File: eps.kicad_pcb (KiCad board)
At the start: 4 copper layers, 95.9 x 90.2 mm, 141 parts, among them J1 CONN_01X05, J2 CONN_01X05, J3 CONN_01X05, J4 CONN_01X05, J5 +BATT, J6 -BATT, J7 PROGRAMMING PORT, J8 H_EPS, J9 DEBUG, Q1 BSC026NE2LS5, Q2 BSC026NE2LS5, Q3 BSC026NE2LS5, Q4 BSC026NE2LS5, Q5 BSC026NE2LS5, Q6 BSC026NE2LS5, SW1 SW_RST, U1 ATMEGA32M1-MU, U10 ADS7952, U11 TPS630250, U12 bq297xx, U13 INA214, U14 INA214, U15 TPS630250, U16 TPS61088, U17 TPS61088, U18 ADS7952, U19 INA214, U2 INA214, U20 INA214, U21 INA214, U22 REF5025, U23 REF5025, U3 INA214, U4 INA214, U5 INA214, U6 ADA4891-4, U7 ADA4891-4, U8 SN65HVD230, U9 SST25VF016B, Y1 8MHz

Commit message: Merge remote-tracking branch 'origin/master'
# Conflicts:
#	Board.zip
#	Board/eps-B.Cu.gbr
#	Board/eps-B.Mask.gbr
#	Board/eps-B.SilkS.gbr
#	Board/eps-Edge.Cuts.gbr
#	Board/eps-F.Cu.gbr
#	Board/eps-F.Mask.gbr
#	Board/eps-F.SilkS.gbr
#	Board/eps-GND.gbr
#	Board/eps-VCC.gbr
#	Board/eps.drl
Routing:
- net GND: track 327.1 -> 335.0 mm, vias 56 -> 63
- net (no net): vias 4 -> 0
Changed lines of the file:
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@@
     (links 467)
     (no_connects 44)
-    (area 100.034999 49.754999 196.075001 140.075001)
+    (area 98.589999 47.237143 197.520002 141.520002)
     (thickness 1.6)
     (drawings 5)
-    (tracks 1822)
+    (tracks 1832)
     (zones 0)
     (modules 141)
@@
       (padsonsilk false)
       (subtractmaskfromsilk false)
-      (outputformat 2)
+      (outputformat 1)
       (mirror false)
       (drillshape 0)
@@
   (gr_line (start 196 49.83) (end 100.11 49.83) (angle 90) (layer Edge.Cuts) (width 0.15))
   (gr_line (start 196 49.83) (end 196 140) (angle 90) (layer Edge.Cuts) (width 0.15))
-  (via (at 105.19 131.11) (size 6.4) (drill 3.2) (layers F.Cu B.Cu) (net 0))
-  (via (at 105.19 57.45) (size 6.4) (drill 3.2) (layers F.Cu B.Cu) (net 0))
-  (via (at 190.92 134.92) (size 6.4) (drill 3.2) (layers F.Cu B.Cu) (net 0))
-  (via (at 190.92 54.91) (size 6.4) (drill 3.2) (layers F.Cu B.Cu) (net 0))
+  (via (at 105.19 131.11) (size 6.4) (drill 3.2) (layers F.Cu B.Cu) (net 1))
+  (via (at 190.92 54.91) (size 6.4) (drill 3.2) (layers F.Cu B.Cu) (net 1))
+  (segment (start 188.9 74.13) (end 188.9 73.405) (width 0.25) (layer F.Cu) (net 1))
+  (via (at 190.92 134.92) (size 6.4) (drill 3.2) (layers F.Cu B.Cu) (net 1))
+  (via (at 105.19 57.45) (size 6.4) (drill 3.2) (layers F.Cu B.Cu) (net 1))
+  (segment (start 106.35 112.31) (end 106.35 108.59) (width 0.25) (layer F.Cu) (net 1))
+  (segment (start 106.35 108.59) (end 106.67 108.27) (width 0.25) (layer F.Cu) (net 1))
+  (via (at 106.67 108.27) (size 0.6) (drill 0.3) (layers F.Cu B.Cu) (net 1))
+  (segment (start 106.35 117.31) (end 106.35 118.11) (width 0.25) (layer F.Cu) (net 1))
+  (segment (start 106.35 118.11) (end 106.67 118.43) (width 0.25) (layer F.Cu) (net 1))
+  (via (at 106.67 118.43) (size 0.6) (drill 0.3) (layers F.Cu B.Cu) (net 1))
+  (segment (start 106.35 74.13) (end 106.35 73.03) (width 0.25) (layer F.Cu) (net 1))
+  (segment (start 106.35 73.03) (end 106.67 72.71) (width 0.25) (layer F.Cu) (net 1))
+  (via (at 106.67 72.71) (size 0.6) (drill 0.3) (layers F.Cu B.Cu) (net 1))
+  (segment (start 188.9 117.23) (end 188.9 120.02) (width 0.25) (layer F.Cu) (net 1))
+  (segment (start 188.9 120.02) (end 187.95 120.97) (width 0.25) (layer F.Cu) (net 1))
+  (via (at 187.95 120.97) (size 0.6) (drill 0.3) (layers F.Cu B.Cu) (net 1))
+  (segment (start 188.9 112.23) (end 191.61 112.23) (width 0.25) (layer F.Cu) (net 1))
+  (segment (start 191.61 112.23) (end 193.03 110.81) (width 0.25) (layer F.Cu) (net 1))
+  (via (at 193.03 110.81) (size 0.6) (drill 0.3) (layers F.Cu B.Cu) (net 1))
+  (segment (start 188.9 79.13) (end 188.9 81.92) (width 0.25) (layer F.Cu) (net 1))
+  (segment (start 188.9 81.92) (end 187.95 82.87) (width 0.25) (layer F.Cu) (net 1))
+  (via (at 187.95 82.87) (size 0.6) (drill 0.3) (layers F.Cu B.Cu) (net 1))
   (segment (start 138.73754 84.60496) (end 138.73754 84.12998) (width 0.25) (layer F.Cu) (net 1))
   (segment (start 136.35756 81.75) (end 136.26 81.75) (width 0.25) (layer F.Cu) (net 1))
@@
   (segment (start 153.08 56.09) (end 152.07 55.08) (width 0.25) (layer F.Cu) (net 1))
   (via (at 152.07 55.08) (size 0.6) (drill 0.3) (layers F.Cu B.Cu) (net 1))
-  (segment (start 106.35 74.13) (end 106.35 71.59) (width 0.25) (layer GND) (net 1))
-  (via (at 106.35 71.59) (size 0.6) (drill 0.3) (layers F.Cu B.Cu) (net 1))
   (segment (start 106.35 79.13) (end 106.35 81.75) (width 0.25) (layer F.Cu) (net 1))
   (via (at 106.35 81.75) (size 0.6) (drill 0.3) (layers F.Cu B.Cu) (net 1))
@@
   (segment (start 135.56 81.75) (end 133.65 81.75) (width 0.25) (layer F.Cu) (net 1))
   (segment (start 133.65 81.75) (end 133.02 81.12) (width 0.25) (layer F.Cu) (net 1))
-  (segment (start 188.9 79.13) (end 188.9 80.48) (width 0.25) (layer GND) (net 1))
   (segment (start 188.9 74.13) (end 188.9 73.113874) (width 0.25) (layer F.Cu) (net 1))
   (segment (start 188.9 73.113874) (end 188.773063 72.986937) (width 0.25) (layer F.Cu) (net 1))
   (via (at 188.773063 72.986937) (size 0.6) (drill 0.3) (layers F.Cu B.Cu) (net 1))
   (via (at 188.9 74.13) (size 0.6) (drill 0.3) (layers F.Cu B.Cu) (net 1))
-  (segment (start 190.17 112.23) (end 188.9 112.23) (width 0.25) (layer F.Cu) (net 1))
-  (segment (start 190.17 118.58) (end 190.17 116.88) (width 0.25) (layer B.Cu) (net 1))
-  (segment (start 190.17 116.88) (end 190.17 112.23) (width 0.25) (layer B.Cu) (net 1))
-  (via (at 190.17 112.23) (size 0.6) (drill 0.3) (layers F.Cu B.Cu) (net 1))
-  (segment (start 188.9 118.58) (end 190.17 118.58) (width 0.25) (layer B.Cu) (net 1))
   (segment (start 188.9 117.23) (end 188.9 118.58) (width 0.25) (layer F.Cu) (net 1))
-  (via (at 188.9 118.58) (size 0.6) (drill 0.3) (layers F.Cu B.Cu) (net 1))
   (via (at 188.9 117.23) (size 0.6) (drill 0.3) (layers F.Cu B.Cu) (net 1))
   (via (at 188.9 117.23) (size 0.6) (drill 0.3) (layers F.Cu B.Cu) (net 1))
@@
   (segment (start 105.08 120.29) (end 105.08 108.4) (width 0.25) (layer F.Cu) (net 137))
   (segment (start 105.08 108.4) (end 106.35 107.13) (width 0.25) (layer F.Cu) (net 137))
-  (segment (start 109.009968 59.71) (end 109.009968 58.770032) (width 0.25) (layer F.Cu) (net 138))
-  (segment (start 109.009968 58.770032) (end 110.16 57.62) (width 0.25) (layer F.Cu) (net 138))
-  (segment (start 108.119869 71.520131) (end 108.119869 60.600099) (width 0.25) (layer F.Cu) (net 138))
-  (segment (start 108.119869 60.600099) (end 109.009968 59.71) (width 0.25) (layer F.Cu) (net 138))
-  (segment (start 107.62 71.578616) (end 108.061384 71.578616) (width 0.25) (layer F.Cu) (net 138))
-  (segment (start 108.061384 71.578616) (end 108.119869 71.520131) (width 0.25) (layer F.Cu) (net 138))
+  (segment (start 110.16 57.62) (end 109.009968 58.770032) (width 0.25) (layer F.Cu) (net 138))
+  (segment (start 109.009968 58.770032) (end 109.009968 59.71) (width 0.25) (layer F.Cu) (net 138))
+  (segment (start 106.369999 72.084999) (end 105.39999 73.055008) (width 0.25) (layer F.Cu) (net 138))
+  (segment (start 109.009968 59.71) (end 108.119869 60.600099) (width 0.25) (layer F.Cu) (net 138))
+  (segment (start 105.39999 73.055008) (end 105.39999 83.88499) (width 0.25) (layer F.Cu) (net 138))
+  (segment (start 108.119869 60.600099) (end 108.119869 71.520131) (width 0.25) (layer F.Cu) (net 138))
+  (segment (start 107.555001 72.084999) (end 106.369999 72.084999) (width 0.25) (layer F.Cu) (net 138))
+  (segment (start 108.119869 71.520131) (end 107.555001 72.084999) (width 0.25) (layer F.Cu) (net 138))
+  (segment (start 105.39999 83.88499) (end 106.35 84.835) (width 0.25) (layer F.Cu) (net 138))
+  (segment (start 106.35 84.835) (end 106.35 85.56) (width 0.25) (layer F.Cu) (net 138))
   (segment (start 107.62 83.02) (end 107.62 84.44) (width 0.25) (layer F.Cu) (net 138))
   (segment (start 107.62 84.44) (end 106.5 85.56) (width 0.25) (layer F.Cu) (net 138))
@@
   (segment (start 114.19 62.68) (end 111.37 62.68) (width 0.25) (layer B.Cu) (net 138))
   (segment (start 111.37 62.68) (end 111.34 62.71) (width 0.25) (layer B.Cu) (net 138))
-  (segment (start 106.35 85.56) (end 106.35 84.835) (width 0.25) (layer F.Cu) (net 138))
-  (segment (start 106.35 84.835) (end 105.39999 83.88499) (width 0.25) (layer F.Cu) (net 138))
-  (segment (start 105.39999 83.88499) (end 105.39999 73.798626) (width 0.25) (layer F.Cu) (net 138))
-  (segment (start 105.39999 73.798626) (end 107.62 71.578616) (width 0.25) (layer F.Cu) (net 138))
   (segment (start 110.16 57.62) (end 111.15 58.61) (width 0.25) (layer B.Cu) (net 138))
   (segment (start 111.15 58.61) (end 114.19 58.61) (width 0.25) (layer B.Cu) (net 138))

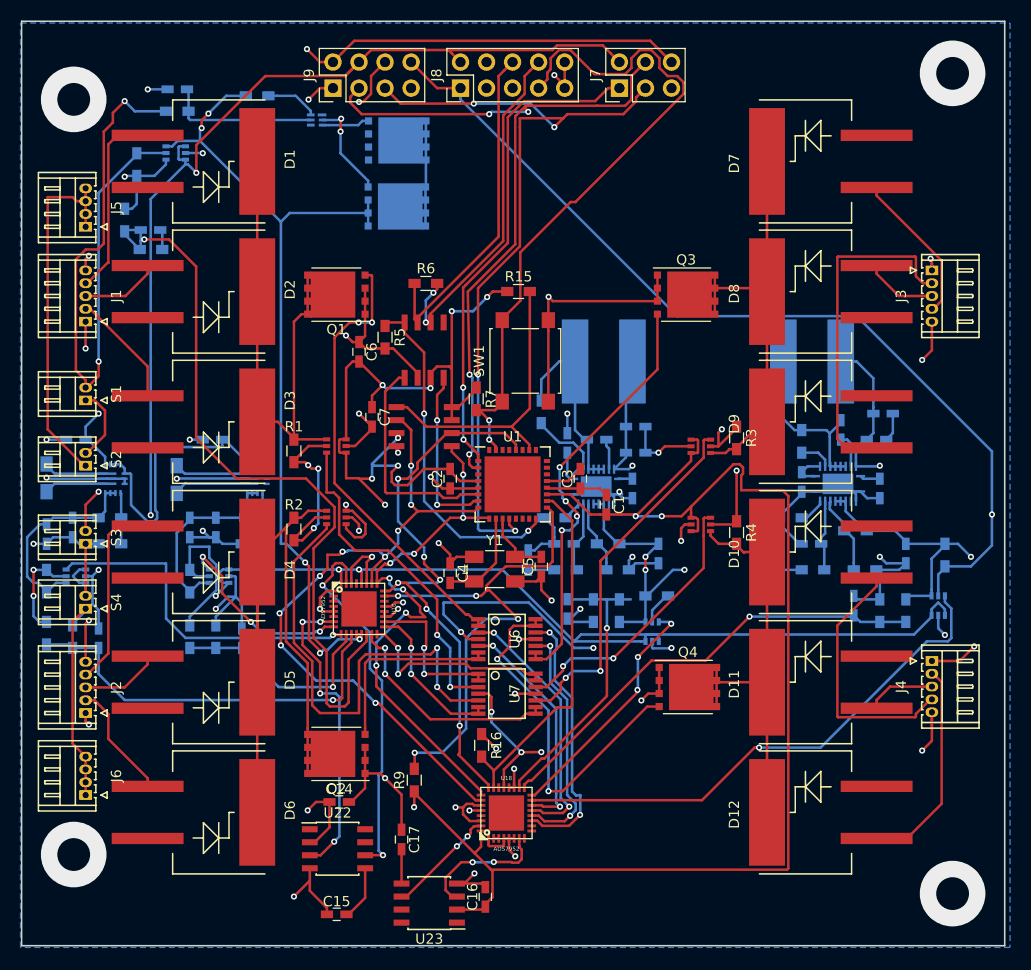
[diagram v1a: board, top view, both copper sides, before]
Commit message: Ground Pour, Pad Clearance
Fixed the ground pour, fixed pad clearances on connectors because DFMcheck was mad about it
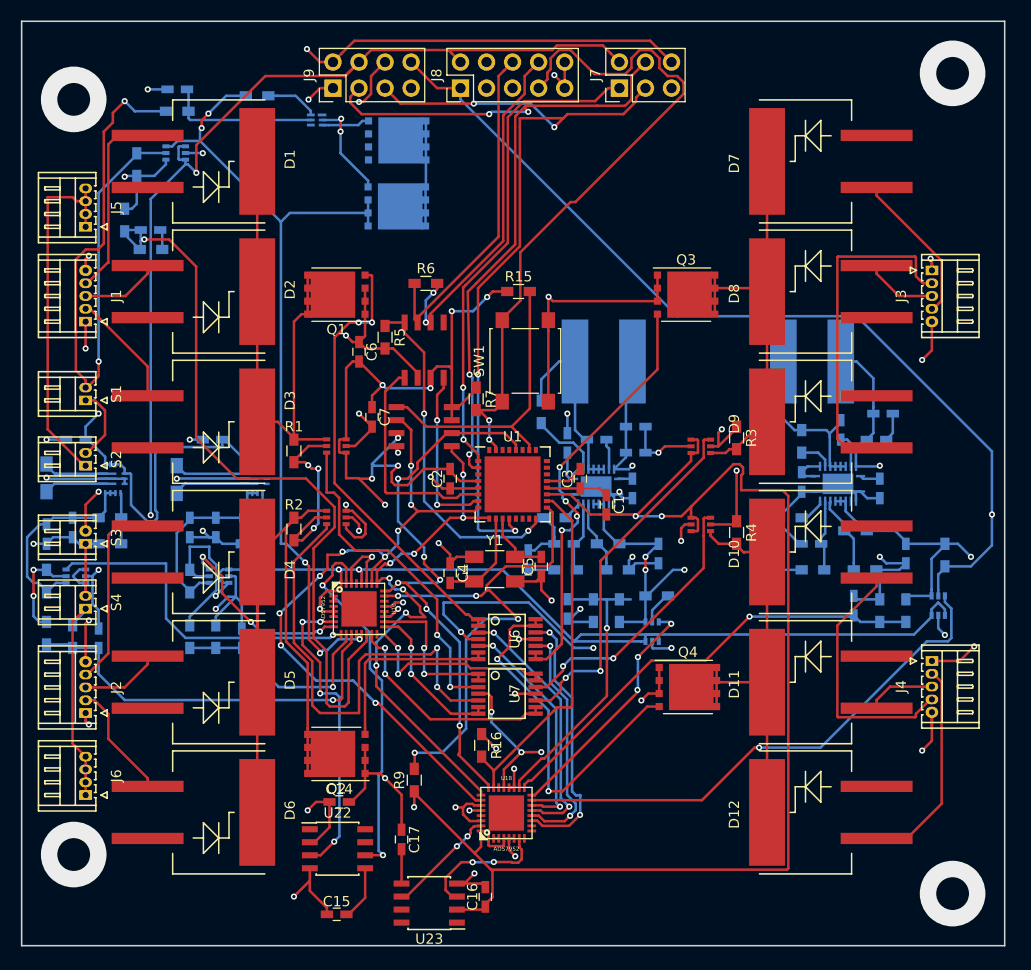
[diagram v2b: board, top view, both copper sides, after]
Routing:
- net GND: vias 63 -> 59
- net (no net): vias 0 -> 4
- added copper zone on GND, net GND
- removed copper zone on B.Cu, net GND
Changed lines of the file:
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@@
-(kicad_pcb (version 4) (host pcbnew 4.0.7)
+(kicad_pcb (version 4) (host pcbnew 4.0.6)
   (general
     (links 467)
-    (no_connects 44)
+    (no_connects 33)
     (area 98.589999 47.237143 197.520002 141.520002)
     (thickness 1.6)
@@
     (2 GND power)
     (31 B.Cu signal)
-    (32 B.Adhes user)
-    (33 F.Adhes user)
-    (34 B.Paste user)
-    (35 F.Paste user)
-    (36 B.SilkS user)
-    (37 F.SilkS user)
-    (38 B.Mask user)
-    (39 F.Mask user)
-    (40 Dwgs.User user)
-    (41 Cmts.User user)
-    (42 Eco1.User user)
-    (43 Eco2.User user)
+    (32 B.Adhes user hide)
+    (33 F.Adhes user hide)
+    (34 B.Paste user hide)
+    (35 F.Paste user hide)
+    (36 B.SilkS user hide)
+    (37 F.SilkS user hide)
+    (38 B.Mask user hide)
+    (39 F.Mask user hide)
+    (40 Dwgs.User user hide)
+    (41 Cmts.User user hide)
+    (42 Eco1.User user hide)
+    (43 Eco2.User user hide)
     (44 Edge.Cuts user)
-    (45 Margin user)
-    (46 B.CrtYd user)
-    (47 F.CrtYd user)
-    (48 B.Fab user)
-    (49 F.Fab user)
+    (45 Margin user hide)
+    (46 B.CrtYd user hide)
+    (47 F.CrtYd user hide)
+    (48 B.Fab user hide)
+    (49 F.Fab user hide)
   )
   (setup
@@
     (mod_text_size 1 1)
     (mod_text_width 0.15)
-    (pad_size 11 11)
-    (pad_drill 6.4)
+    (pad_size 1.1 1.25)
+    (pad_drill 0.6)
     (pad_to_mask_clearance 0.2)
     (aux_axis_origin 0 0)
@@
     (pad 4 thru_hole oval (at 3.75 0 90) (size 0.95 1.25) (drill 0.6) (layers *.Cu *.Mask)
       (net 6 "Net-(D1-Pad1)"))
-    (pad 5 thru_hole oval (at 5 0 90) (size 0.95 1.25) (drill 0.6) (layers *.Cu *.Mask)
+    (pad 5 thru_hole oval (at 5 0 90) (size 1.1 1.25) (drill 0.6) (layers *.Cu *.Mask)
       (net 1 GND))
     (model ${KISYS3DMOD}/Connectors_Hirose.3dshapes/Hirose_DF13-05P-1.25DS_05x1.25mm_Angled.wrl
@@
     (pad 4 thru_hole oval (at 3.75 0 90) (size 0.95 1.25) (drill 0.6) (layers *.Cu *.Mask)
       (net 13 "Net-(D4-Pad1)"))
-    (pad 5 thru_hole oval (at 5 0 90) (size 0.95 1.25) (drill 0.6) (layers *.Cu *.Mask)
+    (pad 5 thru_hole oval (at 5 0 90) (size 1.1 1.25) (drill 0.6) (layers *.Cu *.Mask)
       (net 1 GND))
     (model ${KISYS3DMOD}/Connectors_Hirose.3dshapes/Hirose_DF13-05P-1.25DS_05x1.25mm_Angled.wrl
@@
     (pad 4 thru_hole oval (at 3.75 0 270) (size 0.95 1.25) (drill 0.6) (layers *.Cu *.Mask)
       (net 20 "Net-(D7-Pad1)"))
-    (pad 5 thru_hole oval (at 5 0 270) (size 0.95 1.25) (drill 0.6) (layers *.Cu *.Mask)
+    (pad 5 thru_hole oval (at 5 0 270) (size 1.1 1.25) (drill 0.6) (layers *.Cu *.Mask)
       (net 1 GND))
     (model ${KISYS3DMOD}/Connectors_Hirose.3dshapes/Hirose_DF13-05P-1.25DS_05x1.25mm_Angled.wrl
@@
     (pad 4 thru_hole oval (at 3.75 0 270) (size 0.95 1.25) (drill 0.6) (layers *.Cu *.Mask)
       (net 27 "Net-(D10-Pad1)"))
-    (pad 5 thru_hole oval (at 5 0 270) (size 0.95 1.25) (drill 0.6) (layers *.Cu *.Mask)
+    (pad 5 thru_hole oval (at 5 0 270) (size 1.1 1.25) (drill 0.6) (layers *.Cu *.Mask)
       (net 1 GND))
     (model ${KISYS3DMOD}/Connectors_Hirose.3dshapes/Hirose_DF13-05P-1.25DS_05x1.25mm_Angled.wrl
@@
     (pad 1 thru_hole rect (at 0 0 90) (size 0.95 1.25) (drill 0.6) (layers *.Cu *.Mask)
       (net 140 "Net-(S3-Pad1)"))
-    (pad 2 thru_hole oval (at 1.25 0 90) (size 0.95 1.25) (drill 0.6) (layers *.Cu *.Mask)
+    (pad 2 thru_hole oval (at 1.25 0 90) (size 1.1 1.25) (drill 0.6) (layers *.Cu *.Mask)
       (net 1 GND))
     (model ${KISYS3DMOD}/Connectors_Hirose.3dshapes/Hirose_DF13-02P-1.25DS_02x1.25mm_Angled.wrl
@@
   (gr_line (start 196 49.83) (end 100.11 49.83) (angle 90) (layer Edge.Cuts) (width 0.15))
   (gr_line (start 196 49.83) (end 196 140) (angle 90) (layer Edge.Cuts) (width 0.15))
-  (via (at 105.19 131.11) (size 6.4) (drill 3.2) (layers F.Cu B.Cu) (net 1))
-  (via (at 190.92 54.91) (size 6.4) (drill 3.2) (layers F.Cu B.Cu) (net 1))
+  (via (at 105.19 131.11) (size 6.4) (drill 3.2) (layers F.Cu B.Cu) (net 0))
+  (via (at 190.92 54.91) (size 6.4) (drill 3.2) (layers F.Cu B.Cu) (net 0))
+  (via (at 190.92 134.92) (size 6.4) (drill 3.2) (layers F.Cu B.Cu) (net 0))
+  (via (at 105.19 57.45) (size 6.4) (drill 3.2) (layers F.Cu B.Cu) (net 0))
   (segment (start 188.9 74.13) (end 188.9 73.405) (width 0.25) (layer F.Cu) (net 1))
-  (via (at 190.92 134.92) (size 6.4) (drill 3.2) (layers F.Cu B.Cu) (net 1))
-  (via (at 105.19 57.45) (size 6.4) (drill 3.2) (layers F.Cu B.Cu) (net 1))
   (segment (start 106.35 112.31) (end 106.35 108.59) (width 0.25) (layer F.Cu) (net 1))
   (segment (start 106.35 108.59) (end 106.67 108.27) (width 0.25) (layer F.Cu) (net 1))
@@
   (segment (start 137.645 135.21) (end 142.555 130.3) (width 0.25) (layer F.Cu) (net 149))
   (via (at 142.57 130.3) (size 0.6) (drill 0.3) (layers F.Cu B.Cu) (net 149))
-  (zone (net 1) (net_name GND) (layer B.Cu) (hatch edge 0.508)
+  (zone (net 60) (net_name +PACK) (layer VCC) (hatch edge 0.508)
     (connect_pads (clearance 0.508))
     (min_thickness 0.254)
@@
     (polygon
       (pts
-        (xy 196.52 140.17) (xy 100 140.17) (xy 100 50) (xy 196.52 50)
+        (xy 196.52 94.45) (xy 100 94.45) (xy 100 50) (xy 196.52 50)
       )
     )
   )
-  (zone (net 60) (net_name +PACK) (layer VCC) (hatch edge 0.508)
+  (zone (net 2) (net_name +3V3) (layer VCC) (hatch edge 0.508)
     (connect_pads (clearance 0.508))
     (min_thickness 0.254)
@@
     (polygon
       (pts
-        (xy 196.52 94.45) (xy 100 94.45) (xy 100 50) (xy 196.52 50)
+        (xy 100 95.72) (xy 100 140.17) (xy 146.99 140.17) (xy 146.99 95.72)
       )
     )
   )
-  (zone (net 2) (net_name +3V3) (layer VCC) (hatch edge 0.508)
+  (zone (net 64) (net_name +5V) (layer VCC) (hatch edge 0.508)
     (connect_pads (clearance 0.508))
     (min_thickness 0.254)
@@
     (polygon
       (pts
-        (xy 100 95.72) (xy 100 140.17) (xy 146.99 140.17) (xy 146.99 95.72)
+        (xy 149.53 95.72) (xy 149.53 140.17) (xy 196.52 140.17) (xy 196.52 95.72)
       )
     )
   )
-  (zone (net 64) (net_name +5V) (layer VCC) (hatch edge 0.508)
+  (zone (net 1) (net_name GND) (layer GND) (hatch edge 0.508)
     (connect_pads (clearance 0.508))
     (min_thickness 0.254)
@@
     (polygon
       (pts
-        (xy 149.53 95.72) (xy 149.53 140.17) (xy 196.52 140.17) (xy 196.52 95.72)
+        (xy 196.02 140.05) (xy 196.01 49.87) (xy 100.09 49.82) (xy 100.12 140.01)
       )
     )

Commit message: repour again
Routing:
- net GND: track 335.0 -> 341.7 mm, vias 59 -> 63
- net (no net): vias 4 -> 0
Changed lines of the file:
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@@
     (thickness 1.6)
     (drawings 5)
-    (tracks 1832)
+    (tracks 1838)
     (zones 0)
     (modules 141)
@@
   (gr_line (start 196 49.83) (end 100.11 49.83) (angle 90) (layer Edge.Cuts) (width 0.15))
   (gr_line (start 196 49.83) (end 196 140) (angle 90) (layer Edge.Cuts) (width 0.15))
-  (via (at 105.19 131.11) (size 6.4) (drill 3.2) (layers F.Cu B.Cu) (net 0))
-  (via (at 190.92 54.91) (size 6.4) (drill 3.2) (layers F.Cu B.Cu) (net 0))
-  (via (at 190.92 134.92) (size 6.4) (drill 3.2) (layers F.Cu B.Cu) (net 0))
-  (via (at 105.19 57.45) (size 6.4) (drill 3.2) (layers F.Cu B.Cu) (net 0))
+  (segment (start 105.16 131.11) (end 104.98 131.11) (width 0.25) (layer B.Cu) (net 1))
+  (segment (start 105.19 131.14) (end 105.16 131.11) (width 0.25) (layer B.Cu) (net 1))
+  (via (at 105.19 131.14) (size 6.4) (drill 3.2) (layers F.Cu B.Cu) (net 1))
+  (via (at 105.19 57.45) (size 5.4) (drill 3.2) (layers F.Cu B.Cu) (net 1))
+  (via (at 112.41 56.47) (size 0.6) (drill 0.3) (layers F.Cu B.Cu) (net 1))
+  (segment (start 112.41 56.47) (end 114.34 56.47) (width 0.25) (layer B.Cu) (net 1))
+  (segment (start 190.41 55.42) (end 190.92 54.91) (width 0.25) (layer GND) (net 1))
+  (segment (start 190.41 55.42) (end 190.92 54.91) (width 0.25) (layer GND) (net 1))
+  (segment (start 188.9 56.93) (end 190.41 55.42) (width 0.25) (layer GND) (net 1))
+  (via (at 190.92 54.91) (size 6.4) (drill 3.2) (layers F.Cu B.Cu) (net 1))
+  (segment (start 188.9 132.9) (end 190.92 134.92) (width 0.25) (layer GND) (net 1))
+  (via (at 190.92 134.92) (size 6.4) (drill 3.2) (layers F.Cu B.Cu) (net 1))
   (segment (start 188.9 74.13) (end 188.9 73.405) (width 0.25) (layer F.Cu) (net 1))
   (segment (start 106.35 112.31) (end 106.35 108.59) (width 0.25) (layer F.Cu) (net 1))
@@
   (segment (start 128.22 133.66) (end 126.67 135.21) (width 0.25) (layer F.Cu) (net 1))
   (via (at 126.67 135.21) (size 0.6) (drill 0.3) (layers F.Cu B.Cu) (net 1))
-  (via (at 112.41 56.47) (size 0.6) (drill 0.3) (layers F.Cu B.Cu) (net 1))
-  (segment (start 114.34 56.47) (end 112.41 56.47) (width 0.25) (layer B.Cu) (net 1))
   (segment (start 163.5 53.81) (end 161.42498 51.73498) (width 0.25) (layer F.Cu) (net 1))
   (segment (start 161.42498 51.73498) (end 132.55502 51.73498) (width 0.25) (layer F.Cu) (net 1))
